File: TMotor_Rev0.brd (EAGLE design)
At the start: 98.9 x 68.7 mm, 33 parts, among them U1 INA125U, U2 INA125U

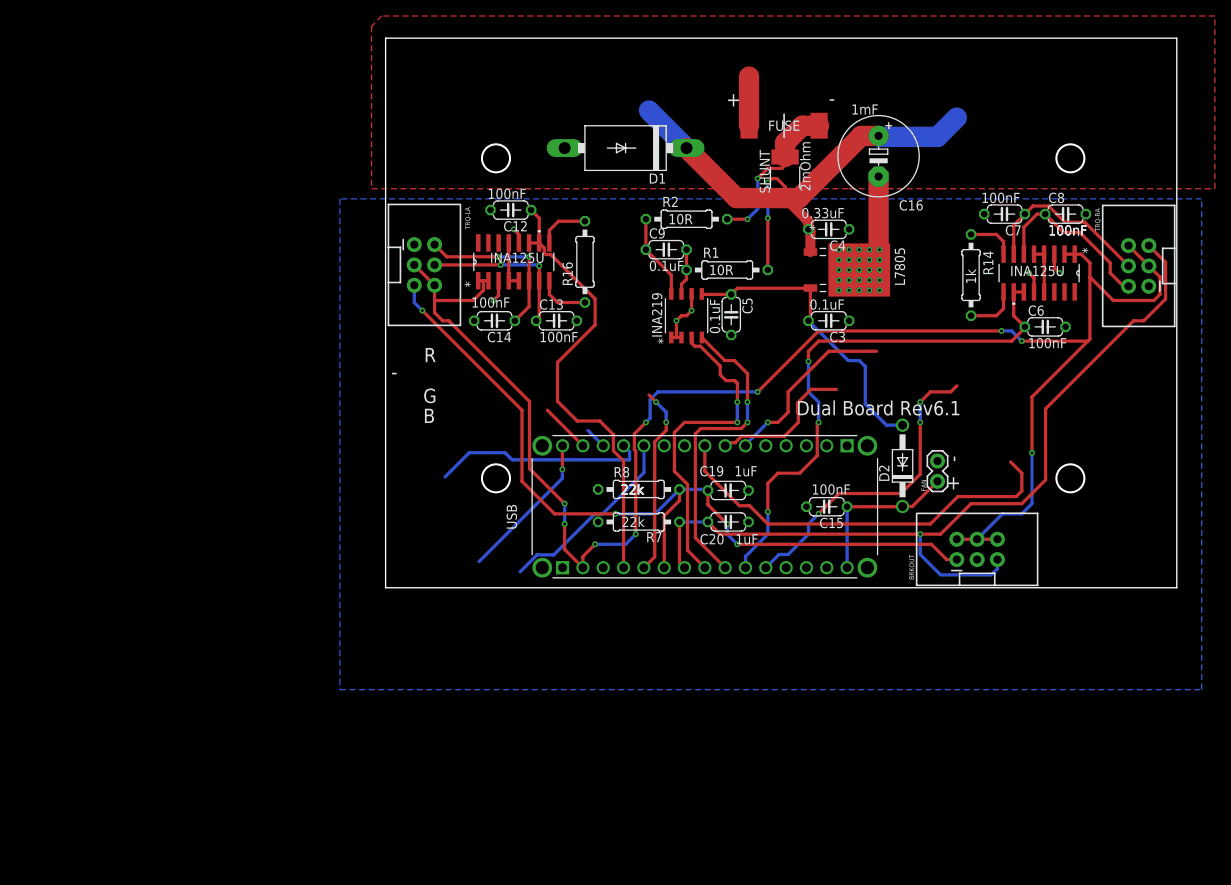
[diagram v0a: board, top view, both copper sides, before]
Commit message: Pre check completion, with pogo pins
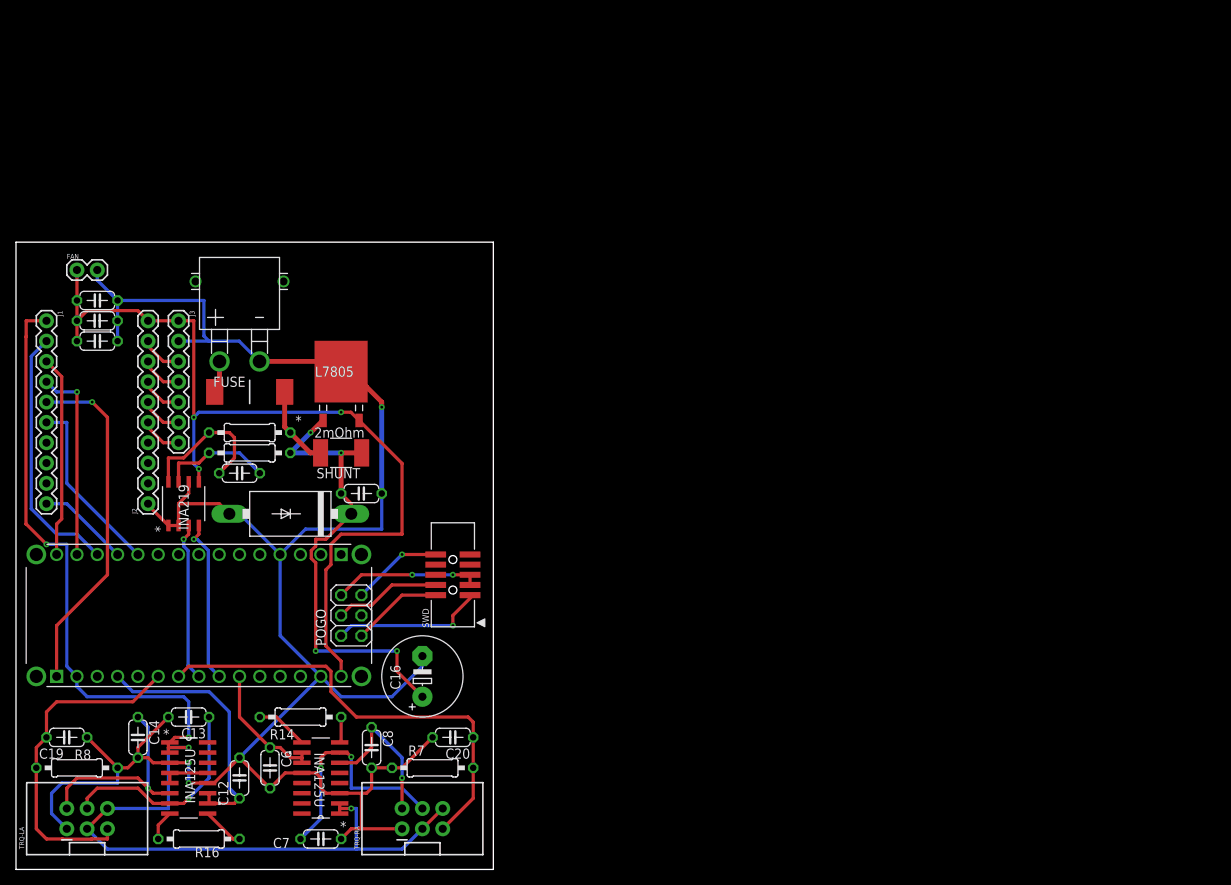
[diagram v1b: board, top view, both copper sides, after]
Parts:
- removed BRKOUT: (no value), SparkFun-Connectors:2X3-SHROUDED
- removed D2: 1N4004, diode:DO41-10
- added J1, J2: (no value), SparkFun-Connectors:1X10
- added J3: (no value), SparkFun-Connectors:1X07
- added POGO: (no value), pinhead:2X03
- added SWD: 20317, microbuilder:2X05_1.27MM_BOX_POSTS
- added U$9: XT30, Ben_Library:XT30_HORIZONTAL
- moved C7 115.8 mm to (38.1, 0.00), turned to 0 degrees
- moved TRQ-RA 113.1 mm to (50.8, 2.54), turned to 90 degrees
- moved C6 111.5 mm to (31.8, 8.89), turned to 270 degrees
- moved FAN 110.8 mm to (7.62, 71.1), turned to 0 degrees
- moved U2 109.8 mm to (38.1, 7.62), turned to 180 degrees
- moved C8 109.4 mm to (44.5, 11.4), turned to 270 degrees
- moved R14 100.4 mm to (35.6, 15.2), turned to 180 degrees
- moved C15 94.8 mm to (10.2, 67.3), turned to 0 degrees
- moved C3 91.4 mm to (10.2, 64.8)
- moved C19 88.2 mm to (6.35, 12.7)
- moved R16 86.8 mm to (22.9, 0.00), turned to 0 degrees
- moved C16 86.5 mm to (50.8, 20.3), turned to 90 degrees
- moved TRQ-LA 81.0 mm to (8.89, 2.54), turned to 90 degrees
- moved C5 79.3 mm to (10.2, 62.2), turned to 0 degrees
- moved C12 78.7 mm to (27.9, 7.62), turned to 90 degrees
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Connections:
- net MD_VCC renamed L7_VIN
- net N$2 renamed PF_VCC
- removed net 5V: C3.2, C5.1, D2.A, INA219.5, L7805.2
- removed net D11: USB.B14
- removed net D12: USB.B15
- removed net D8: USB.B11
- removed net D9: USB.B12
- removed net N$1: FUSE.2
- removed net PWM-RL: USB.B13
- new net CAN_CS: J1.2, USB.B13
- new net CAN_INT: J1.6, USB.B11
- new net H_CS: J2.9, J3.3
- new net H_INT: J2.5, J3.7
- new net H_MISO: J2.8, J3.4
- new net H_MOSI: J2.7, J3.5
- new net H_SCK: J2.6, J3.6
- new net LLS_OE: J1.10, USB.B12
- new net MISO: J1.3, USB.B15
- new net MOSI: J1.4, USB.B14
- new net N$27: J1.7
- new net N$28: J1.8
- new net N$29: J1.9
- new net NRESET: POGO.5, SWD.10
- new net SCK: J1.5, USB.A1
- new net SW3.3V: POGO.2, SWD.1
- new net SWCLK: POGO.4, SWD.4
- new net SWDIO: POGO.1, SWD.2
- new net SWGND: POGO.6, SWD.3, SWD.5
- new net VCC: FUSE.2, U$9.+
- net 3.3V: now also J1.1; no longer BRKOUT.2, BRKOUT.4, BRKOUT.6
- net A2: no longer BRKOUT.1
- net A3: no longer BRKOUT.5
- net GND: now also J2.1, J3.2, U$9.-
- net VIN: now also C3.2, C5.1, INA219.5, J2.10, J3.1, L7805.2; no longer D2.C
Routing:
- net GND: track 30.5 -> 250.2 mm, vias 31 -> 3
- net VIN: track 20.2 -> 109.7 mm, vias 0 -> 3
- net A2: track 103.4 -> 41.6 mm, vias 4 -> 0
- net 3.3V: track 210.3 -> 155.6 mm, vias 9 -> 4
- net D5: track 51.4 -> 0.00 mm
- net A6: track 67.6 -> 16.3 mm, vias 3 -> 0
- net A3: track 107.0 -> 56.9 mm, vias 1 -> 0
- net SCK: track 0.00 -> 43.4 mm, vias 0 -> 1
- net A7: track 39.3 -> 0.00 mm, vias 3 -> 0
- net 5V: track 38.0 -> 0.00 mm
- net CAN_CS: track 0.00 -> 32.4 mm
- net D9: track 26.7 -> 0.00 mm
- net MISO: track 0.00 -> 25.2 mm
- net MOSI: track 0.00 -> 24.7 mm, vias 0 -> 1
- net D8: track 24.0 -> 0.00 mm
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- removed copper zone on layer 1, net GND
- removed copper zone on layer 16, net GND
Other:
- board size 98.9 x 68.7 mm -> 59.7 x 78.4 mm
- board text removed: "+"
- board text removed: "-"
- board text removed: "0.1uF"
- board text removed: "0.33uF"
- board text removed: "100nF"
- board text removed: "10R"
- board text removed: "1k"
- board text removed: "1mF"
- board text removed: "1uF"
- board text removed: "22k"
- board text removed: "B"
- board text removed: "Dual Board Rev6.1"
- board text removed: "G"
- board text removed: "R"
